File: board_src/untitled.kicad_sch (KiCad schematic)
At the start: 3 parts, among them IC3 DS18B20+, J11 Conn_01x03

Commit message: dodany tranzystor BS123
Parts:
- IC3: footprint footprints:DS18B20 -> Package_TO_SOT_THT:TO-92L_Inline_Wide
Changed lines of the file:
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@@
 			)
 		)
-		(property "Footprint" "footprints:DS18B20"
+		(property "Footprint" "Package_TO_SOT_THT:TO-92L_Inline_Wide"
 			(at 139.7 19.38 0)
 			(effects

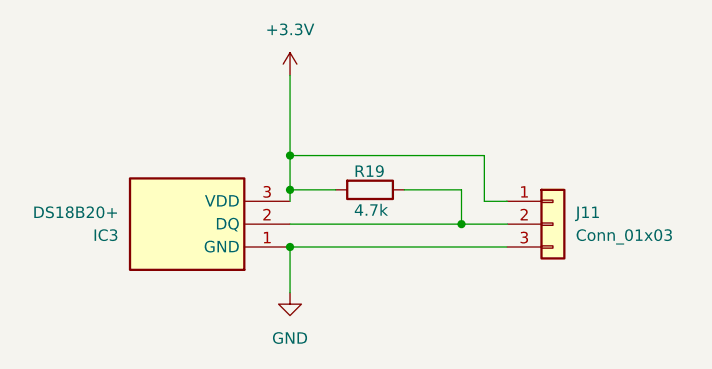
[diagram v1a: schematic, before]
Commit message: Poprawki w schematach. Rozpoczęte korekty płytki
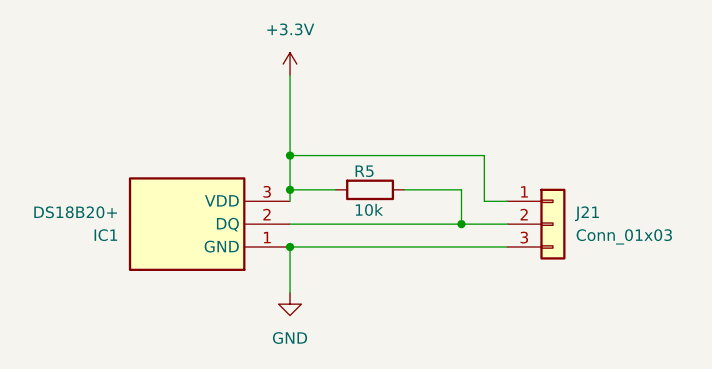
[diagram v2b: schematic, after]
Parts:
- J21: renamed from J11; footprint Connector_PinHeader_2.54mm:PinHeader_1x03_P2.54mm_Vertical -> Connector_PinHeader_2.54mm:PinHeader_2x20_P2.54mm_Vertical
- R5: renamed from R19; value 4.7k -> 10k; footprint Resistor_SMD:R_0603_1608Metric -> Resistor_SMD:R_0603_1608Metric_Pad0.98x0.95mm_HandSolder
- renumbered IC3 to IC1
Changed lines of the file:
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@@
 		(dnp no)
 		(fields_autoplaced yes)
-		(property "Reference" "#PWR016"
+		(property "Reference" "#PWR032"
 			(at 158.75 99.06 0)
 			(effects
@@
 			(project "board"
 				(path "/772e9f49-cfcf-4cf6-843d-0684684f2d4b/4ce4dd53-34e3-426c-821d-561d412e5bd5"
-					(reference "#PWR016")
+					(reference "#PWR032")
 					(unit 1)
 				)
@@
 		(dnp no)
 		(fields_autoplaced yes)
-		(property "Reference" "#PWR04"
+		(property "Reference" "#PWR033"
 			(at 158.75 125.73 0)
 			(effects
@@
 			(project ""
 				(path "/772e9f49-cfcf-4cf6-843d-0684684f2d4b/4ce4dd53-34e3-426c-821d-561d412e5bd5"
-					(reference "#PWR04")
+					(reference "#PWR033")
 					(unit 1)
 				)
@@
 		(on_board yes)
 		(dnp no)
-		(property "Reference" "R19"
+		(property "Reference" "R5"
 			(at 165.862 105.918 90)
 			(effects
@@
 			)
 		)
-		(property "Value" "4.7k"
+		(property "Value" "10k"
 			(at 165.862 110.236 90)
 			(effects
@@
 			)
 		)
-		(property "Footprint" "Resistor_SMD:R_0603_1608Metric"
+		(property "Footprint" "Resistor_SMD:R_0603_1608Metric_Pad0.98x0.95mm_HandSolder"
 			(at 167.64 106.172 90)
 			(effects
@@
 			(project "board"
 				(path "/772e9f49-cfcf-4cf6-843d-0684684f2d4b/4ce4dd53-34e3-426c-821d-561d412e5bd5"
-					(reference "R19")
+					(reference "R5")
 					(unit 1)
 				)
@@
 		(dnp no)
 		(fields_autoplaced yes)
-		(property "Reference" "J11"
+		(property "Reference" "J21"
 			(at 190.5 110.4899 0)
 			(effects
@@
 			)
 		)
-		(property "Footprint" "Connector_PinHeader_2.54mm:PinHeader_1x03_P2.54mm_Vertical"
+		(property "Footprint" "Connector_PinHeader_2.54mm:PinHeader_2x20_P2.54mm_Vertical"
 			(at 187.96 111.76 0)
 			(effects
@@
 			(project "board"
 				(path "/772e9f49-cfcf-4cf6-843d-0684684f2d4b/4ce4dd53-34e3-426c-821d-561d412e5bd5"
-					(reference "J11")
+					(reference "J21")
 					(unit 1)
 				)
@@
 		(dnp no)
 		(fields_autoplaced yes)
-		(property "Reference" "IC3"
+		(property "Reference" "IC1"
 			(at 139.7 113.0301 0)
 			(effects
@@
 			(project ""
 				(path "/772e9f49-cfcf-4cf6-843d-0684684f2d4b/4ce4dd53-34e3-426c-821d-561d412e5bd5"
-					(reference "IC3")
-					(unit 1)
-				)
+					(reference "IC1")
+					(unit 1)
+				)

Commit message: Wprowadzono usprawnienia i poprawki. Wersja ostateczna, wysłana do JLCPCB.
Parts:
- added C13: 100n, Capacitor_SMD:C_0603_1608Metric_Pad1.08x0.95mm_HandSolder, symbol Device:C
- J21: footprint Connector_PinHeader_2.54mm:PinHeader_2x20_P2.54mm_Vertical -> Connector_PinHeader_2.54mm:PinHeader_1x03_P2.54mm_Vertical
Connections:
- net +3.3V: now also C13.1
- net GND: now also C13.2
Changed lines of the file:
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@@
+	)
+	(junction
+		(at 158.75 99.06)
+		(diameter 0)
+		(color 0 0 0 0)
 	)
 	(junction
@@
 	(wire
 		(pts
+			(xy 158.75 99.06) (xy 158.75 104.14)
+		)
+		(stroke
+			(width 0)
+			(type default)
+		)
+	)
+	(wire
+		(pts
 			(xy 177.8 107.95) (xy 177.8 111.76)
 		)
@@
 	(wire
 		(pts
+			(xy 167.64 99.06) (xy 168.91 99.06)
+		)
+		(stroke
+			(width 0)
+			(type default)
+		)
+	)
+	(wire
+		(pts
 			(xy 158.75 114.3) (xy 182.88 114.3)
 		)
@@
 	(wire
 		(pts
-			(xy 158.75 95.25) (xy 158.75 104.14)
+			(xy 158.75 99.06) (xy 160.02 99.06)
+		)
+		(stroke
+			(width 0)
+			(type default)
+		)
+	)
+	(wire
+		(pts
+			(xy 158.75 95.25) (xy 158.75 99.06)
 		)
 		(stroke
@@
 	)
 	(symbol
+		(lib_id "Device:C")
+		(at 163.83 99.06 90)
+		(unit 1)
+		(exclude_from_sim no)
+		(in_bom yes)
+		(on_board yes)
+		(dnp no)
+		(fields_autoplaced yes)
+		(property "Reference" "C13"
+			(at 163.83 91.44 90)
+			(effects
+				(font
+					(size 1.27 1.27)
+				)
+			)
+		)
+		(property "Value" "100n"
+			(at 163.83 93.98 90)
+			(effects
+				(font
+					(size 1.27 1.27)
+				)
+			)
+		)
+		(property "Footprint" "Capacitor_SMD:C_0603_1608Metric_Pad1.08x0.95mm_HandSolder"
+			(at 167.64 98.0948 0)
+			(effects
+				(font
+					(size 1.27 1.27)
+				)
+				(hide yes)
+			)
+		)
+		(property "Datasheet" "~"
+			(at 163.83 99.06 0)
+			(effects
+				(font
+					(size 1.27 1.27)
+				)
+				(hide yes)
+			)
+		)
+		(property "Description" "Unpolarized capacitor"
+			(at 163.83 99.06 0)
+			(effects
+				(font
+					(size 1.27 1.27)
+				)
+				(hide yes)
+			)
+		)
+		(pin "2"
+		)
+		(pin "1"
+		)
+		(instances
+			(project "board"
+				(path "/772e9f49-cfcf-4cf6-843d-0684684f2d4b/4ce4dd53-34e3-426c-821d-561d412e5bd5"
+					(reference "C13")
+					(unit 1)
+				)
+			)
+		)
+	)
+	(symbol
 		(lib_id "Device:R")
 		(at 167.64 107.95 270)
@@
 			)
 		)
-		(property "Footprint" "Connector_PinHeader_2.54mm:PinHeader_2x20_P2.54mm_Vertical"
+		(property "Footprint" "Connector_PinHeader_2.54mm:PinHeader_1x03_P2.54mm_Vertical"
 			(at 187.96 111.76 0)
 			(effects
@@
 					(unit 1)
 				)
+			)
+		)
+	)
+	(symbol
+		(lib_id "power:GND")
+		(at 168.91 99.06 90)
+		(unit 1)
+		(exclude_from_sim no)
+		(in_bom yes)
+		(on_board yes)
+		(dnp no)
+		(fields_autoplaced yes)
+		(property "Reference" "#PWR0120"
+			(at 175.26 99.06 0)
+			(effects
+				(font
+					(size 1.27 1.27)
+				)
+				(hide yes)
+			)
+		)
+		(property "Value" "GND"
+			(at 172.72 99.0599 90)
+			(effects
+				(font
+					(size 1.27 1.27)
+				)
+				(justify right)
+			)
+		)
+		(property "Footprint" ""
+			(at 168.91 99.06 0)
+			(effects
+				(font
+					(size 1.27 1.27)
+				)
+				(hide yes)
+			)
+		)
+		(property "Datasheet" ""
+			(at 168.91 99.06 0)
+			(effects
+				(font
+					(size 1.27 1.27)
+				)
+				(hide yes)
+			)
+		)
+		(property "Description" "Power symbol creates a global label with name \"GND\" , ground"
+			(at 168.91 99.06 0)
+			(effects
+				(font
+					(size 1.27 1.27)
+				)
+				(hide yes)
+			)
+		)
+		(pin "1"
+		)
+		(instances
+			(project "board"
+				(path "/772e9f49-cfcf-4cf6-843d-0684684f2d4b/4ce4dd53-34e3-426c-821d-561d412e5bd5"
+					(reference "#PWR0120")
+					(unit 1)
+				)
